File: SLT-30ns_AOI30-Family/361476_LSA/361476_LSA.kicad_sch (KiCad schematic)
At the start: 7 parts, among them T1 CD, T2 CD, U1 12-Pin_SLx_Can

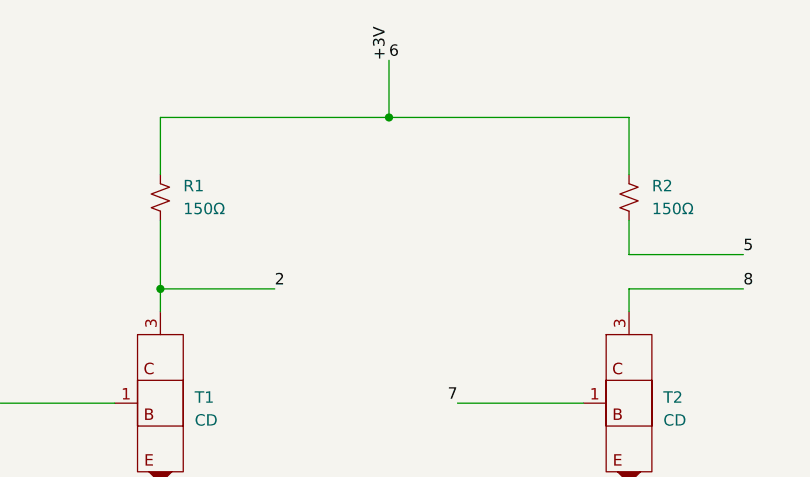
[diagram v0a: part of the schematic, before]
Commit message: Update schematic pdfs
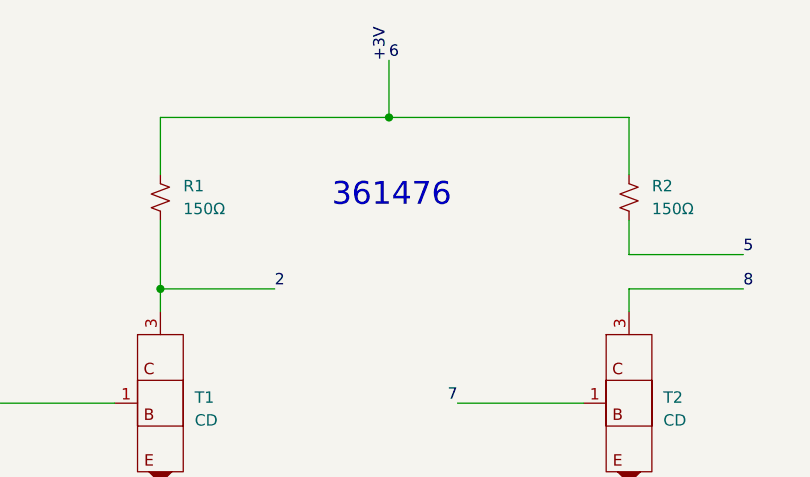
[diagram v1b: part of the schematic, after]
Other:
- note added: "361476"
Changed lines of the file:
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@@
     (stroke (width 0) (type default) (color 0 0 0 0))
+  )
+  (text "361476" (at 109.22 82.55 0)
+    (effects (font (size 2.54 2.54)) (justify left bottom))
   )
   (label "8" (at 154.94 91.44 0)
